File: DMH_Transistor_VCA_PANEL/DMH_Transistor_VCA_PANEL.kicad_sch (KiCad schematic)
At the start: 5 parts, among them J0 Panel_GND_Solder_Wire_Pad

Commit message: Started panel design
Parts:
- added H10, H11, H8, H9: SIGNAL NAME, SynthStuff:Jack_6.35mm_Cutout_v3, symbol SynthStuff:MountingHole_Jack6.35mm_v2
- added H5: Function, SynthStuff:Pot_Cutout_Medium_v2, symbol SynthStuff:MountingHole_Pot
- added H6, H7: Function, SynthStuff:Pot_Cutout_Tiny_attv, symbol SynthStuff:MountingHole_Pot

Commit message: Panel design ongoing
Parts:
- added H12: Offset, SynthStuff:Pot_Cutout_Small, symbol SynthStuff:MountingHole_Pot
- added H13, H14: Function, SynthStuff:Pot_Cutout_Tiny_attv, symbol SynthStuff:MountingHole_Pot
- added H15: Input, SynthStuff:Jack_6.35mm_Cutout_v3, symbol SynthStuff:MountingHole_Jack6.35mm_v2
- added H16: Output, SynthStuff:Jack_6.35mm_Cutout_Output_v6, symbol SynthStuff:MountingHole_Jack6.35mm_v2
- added H17: CV 1, SynthStuff:Jack_6.35mm_Cutout_v3, symbol SynthStuff:MountingHole_Jack6.35mm_v2
- added H18: CV 2, SynthStuff:Jack_6.35mm_Cutout_v3, symbol SynthStuff:MountingHole_Jack6.35mm_v2
- H10: value SIGNAL NAME -> CV 2
- H11: value SIGNAL NAME -> Output; footprint SynthStuff:Jack_6.35mm_Cutout_v3 -> SynthStuff:Jack_6.35mm_Cutout_Output_v6
- H5: value Function -> Offset; footprint SynthStuff:Pot_Cutout_Medium_v2 -> SynthStuff:Pot_Cutout_Small
- H8: value SIGNAL NAME -> Input
- H9: value SIGNAL NAME -> CV 1

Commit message: Front panel ongoing
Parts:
- H13, H6: value Function -> CV 1 Amt
- H14, H7: value Function -> CV 2 Amt
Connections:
- net GND: now also H10.1, H11.1, H12.1, H13.1, H14.1, H15.1, H16.1, H17.1, H18.1, H5.1, H6.1, H7.1, H8.1, H9.1

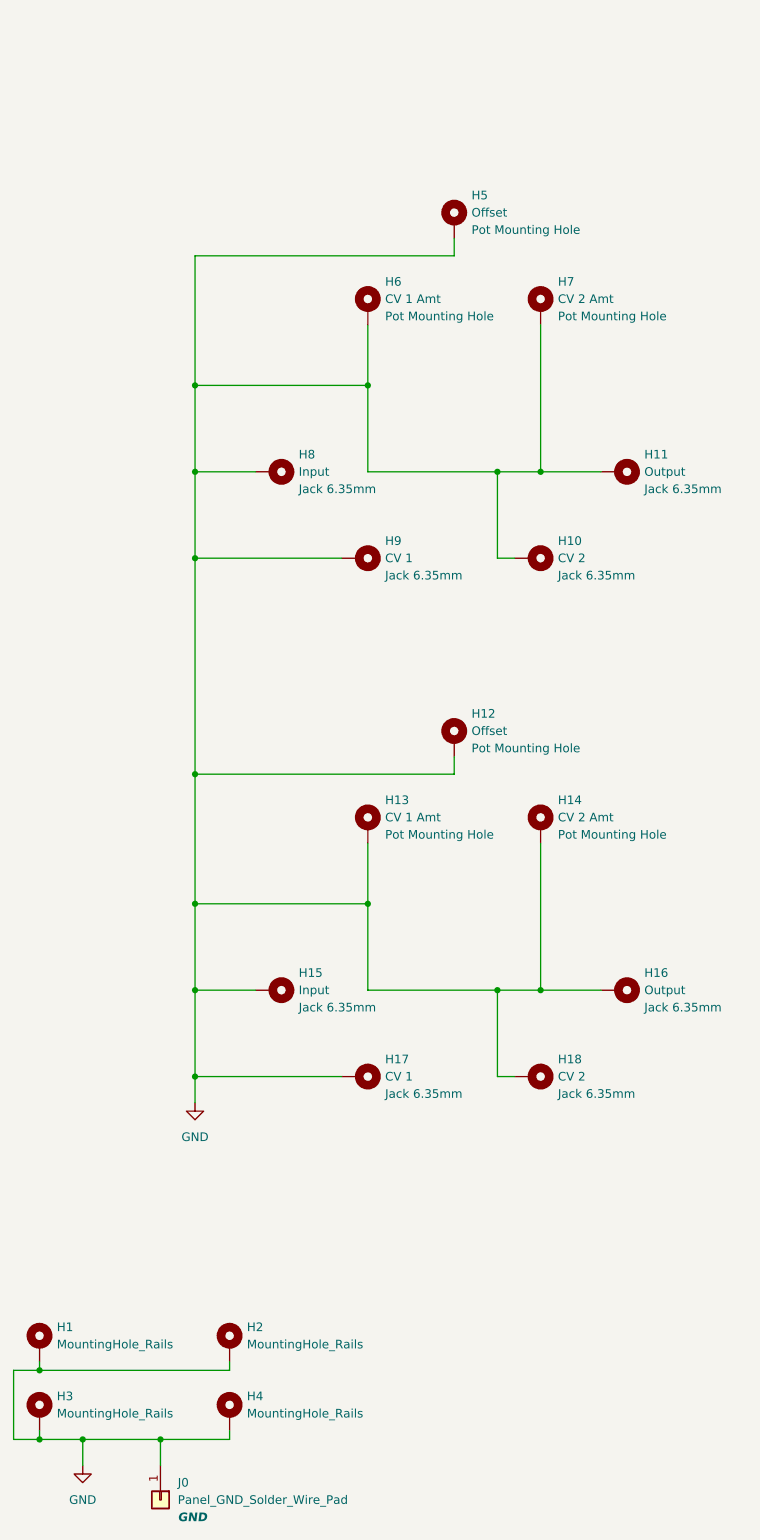
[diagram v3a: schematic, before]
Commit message: Panel experiment in progress
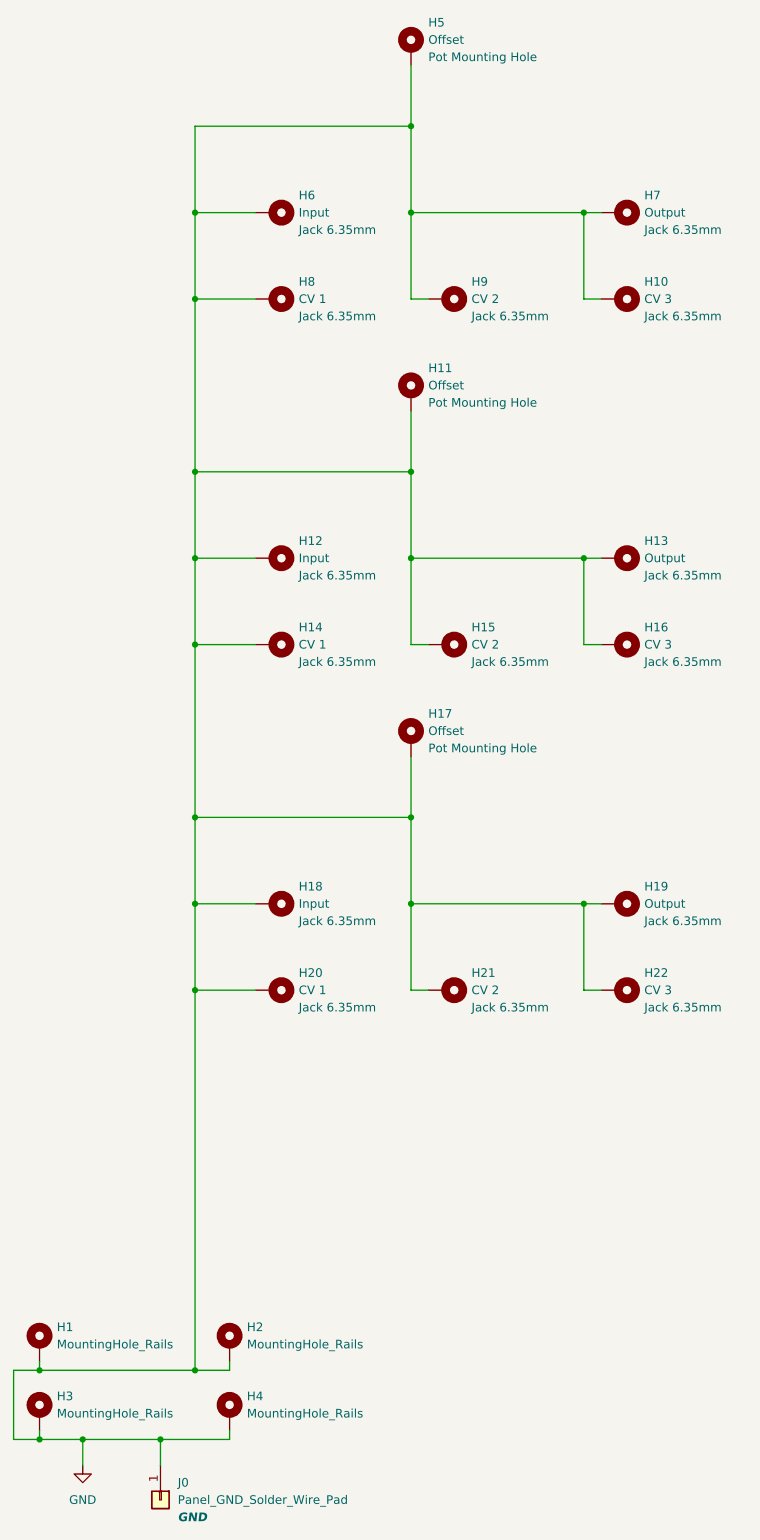
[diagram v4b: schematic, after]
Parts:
- removed H11: Output, SynthStuff:Jack_6.35mm_Cutout_Output_v6, symbol SynthStuff:MountingHole_Jack6.35mm_v2
- removed H13, H6: CV 1 Amt, SynthStuff:Pot_Cutout_Tiny_attv, symbol SynthStuff:MountingHole_Pot
- removed H14, H7: CV 2 Amt, SynthStuff:Pot_Cutout_Tiny_attv, symbol SynthStuff:MountingHole_Pot
- removed H5: Offset, SynthStuff:Pot_Cutout_Small, symbol SynthStuff:MountingHole_Pot
- removed H8: Input, SynthStuff:Jack_6.35mm_Cutout_v3, symbol SynthStuff:MountingHole_Jack6.35mm_v2
- added H11, H17: Offset, SynthStuff:Pot_Cutout_Small, symbol SynthStuff:MountingHole_Pot
- added H12: Input, SynthStuff:Jack_6.35mm_Cutout_v3, symbol SynthStuff:MountingHole_Jack6.35mm_v2
- added H13, H19: Output, SynthStuff:Jack_6.35mm_Cutout_Output_v6, symbol SynthStuff:MountingHole_Jack6.35mm_v2
- added H14, H20: CV 1, SynthStuff:Jack_6.35mm_Cutout_v3, symbol SynthStuff:MountingHole_Jack6.35mm_v2
- added H15, H21: CV 2, SynthStuff:Jack_6.35mm_Cutout_v3, symbol SynthStuff:MountingHole_Jack6.35mm_v2
- added H16, H22: CV 3, SynthStuff:Jack_6.35mm_Cutout_v3, symbol SynthStuff:MountingHole_Jack6.35mm_v2
- H10: value CV 2 -> CV 3
- H18: value CV 2 -> Input
- H9: value CV 1 -> CV 2
- renumbered H12 to H5, H15 to H6, H16 to H7, H17 to H8
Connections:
- net GND: now also H11.1, H12.1, H13.1, H14.1, H15.1, H16.1, H17.1, H19.1, H20.1, H21.1, H22.1
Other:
- moved on the sheet: H5, H6, H7, H8

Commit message: VCM studies
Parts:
- removed H10, H16, H22: CV 3, SynthStuff:Jack_6.35mm_Cutout_v3, symbol SynthStuff:MountingHole_Jack6.35mm_v2
- removed H15: CV 2, SynthStuff:Jack_6.35mm_Cutout_v3, symbol SynthStuff:MountingHole_Jack6.35mm_v2
- H14, H20, H8: value CV 1 -> CV
- H21: value CV 2 -> Mix Out -; footprint SynthStuff:Jack_6.35mm_Cutout_v3 -> SynthStuff:Jack_6.35mm_Cutout_Output_v6
- H9: value CV 2 -> Mix Out +; footprint SynthStuff:Jack_6.35mm_Cutout_v3 -> SynthStuff:Jack_6.35mm_Cutout_Output_v6
